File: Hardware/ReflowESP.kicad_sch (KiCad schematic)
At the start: 64 parts, among them J1 V_SSR_SEL, J2 USB_B_Micro, J3 SSR1, J4 EXT_V_SSR, J5 SSR2, J6 SSR3, J7 TC1, J8 TC2, Q1 BSS138, Q2 BSS138, Q3 S8050, Q4 S8050, Q5 BSS138, SW1 SW_RESET, SW2 SW_BOOT, U1 CH340G, U2 NCP1117-3.3_SOT223, U4 MAX31855KASA, U5 MAX31855KASA, Y1 12MHz

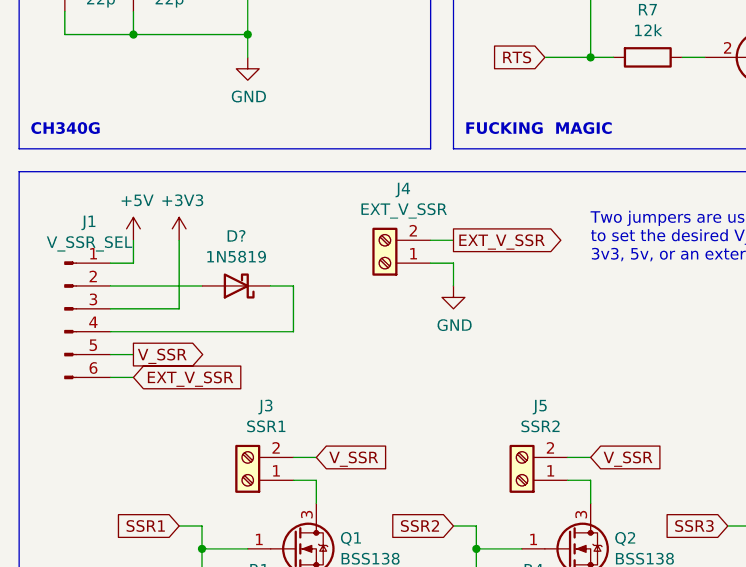
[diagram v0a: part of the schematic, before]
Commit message: Fix V_SSR_SEL
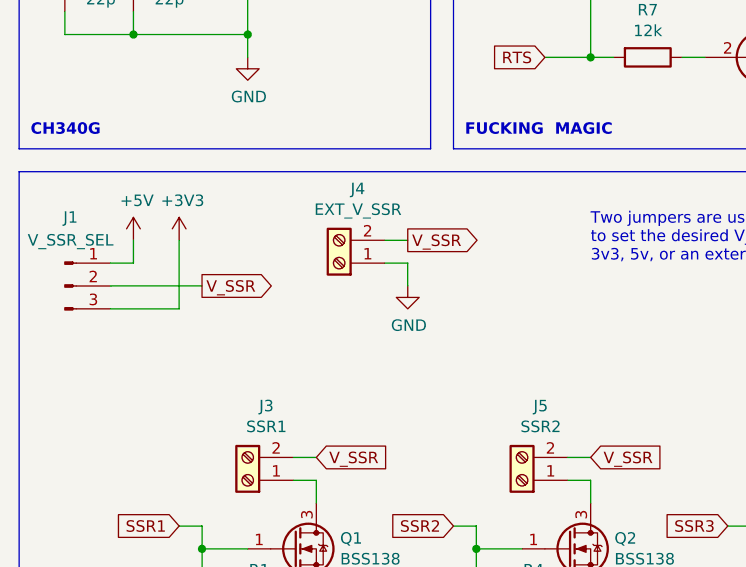
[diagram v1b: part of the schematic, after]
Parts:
- removed D?: 1N5819, Diode_THT:D_DO-41_SOD81_P10.16mm_Horizontal, symbol Diode:1N5819
- removed J1: V_SSR_SEL, symbol Connector:Conn_01x06_Male
- added J1: V_SSR_SEL, symbol Connector:Conn_01x03_Male
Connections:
- net EXT_V_SSR is gone; now on net V_SSR: J4.2 (Pin_2)
- net +3V3: now also J1.3 (Pin_3)
- net +5V: now also J1.1 (Pin_1)
- net V_SSR: now also J1.2 (Pin_2)
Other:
- moved on the sheet: J4
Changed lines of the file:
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@@
-    (stroke (width 0) (type default) (color 0 0 0 0))
-  )
-  (wire (pts (xy 40.64 149.86) (xy 43.18 149.86))
     (stroke (width 0) (type default) (color 0 0 0 0))
   )
@@
     (stroke (width 0) (type default) (color 0 0 0 0))
   )
-  (wire (pts (xy 60.96 147.32) (xy 60.96 149.86))
+  (wire (pts (xy 55.88 147.32) (xy 55.88 149.86))
     (stroke (width 0) (type default) (color 0 0 0 0))
   )
@@
     (stroke (width 0) (type default) (color 0 0 0 0))
   )
-  (wire (pts (xy 25.4 157.48) (xy 22.86 157.48))
-    (stroke (width 0) (type default) (color 0 0 0 0))
-  )
   (wire (pts (xy 200.66 91.44) (xy 203.2 91.44))
     (stroke (width 0) (type default) (color 0 0 0 0))
   )
-  (wire (pts (xy 58.42 147.32) (xy 60.96 147.32))
+  (wire (pts (xy 53.34 147.32) (xy 55.88 147.32))
     (stroke (width 0) (type default) (color 0 0 0 0))
   )
@@
     (stroke (width 0) (type default) (color 0 0 0 0))
   )
-  (wire (pts (xy 22.86 154.94) (xy 43.18 154.94))
-    (stroke (width 0) (type default) (color 0 0 0 0))
-  )
   (wire (pts (xy 45.72 186.69) (xy 45.72 189.23))
     (stroke (width 0) (type default) (color 0 0 0 0))
@@
     (stroke (width 0) (type default) (color 0 0 0 0))
   )
-  (wire (pts (xy 43.18 149.86) (xy 43.18 154.94))
-    (stroke (width 0) (type default) (color 0 0 0 0))
-  )
   (wire (pts (xy 33.02 25.4) (xy 43.18 25.4))
     (stroke (width 0) (type default) (color 0 0 0 0))
@@
     (stroke (width 0) (type default) (color 0 0 0 0))
   )
-  (wire (pts (xy 25.4 160.02) (xy 22.86 160.02))
-    (stroke (width 0) (type default) (color 0 0 0 0))
-  )
   (wire (pts (xy 17.78 111.76) (xy 17.78 114.3))
     (stroke (width 0) (type default) (color 0 0 0 0))
@@
     (stroke (width 0) (type default) (color 0 0 0 0))
   )
-  (wire (pts (xy 60.96 144.78) (xy 58.42 144.78))
+  (wire (pts (xy 55.88 144.78) (xy 53.34 144.78))
     (stroke (width 0) (type default) (color 0 0 0 0))
   )
@@
     )
   )
-  (global_label "EXT_V_SSR" (shape input) (at 25.4 160.02 0) (fields_autoplaced)
-    (effects (font (size 1.27 1.27)) (justify left))
-    (property "Intersheet References" "${INTERSHEET_REFS}" (id 0) (at -5.08 0 0)
-      (effects (font (size 1.27 1.27)) hide)
-    )
-  )
   (global_label "EN" (shape output) (at 109.22 53.34 0) (fields_autoplaced)
     (effects (font (size 1.27 1.27)) (justify left))
@@
     (effects (font (size 1.27 1.27)) (justify right))
     (property "Intersheet References" "${INTERSHEET_REFS}" (id 0) (at 5.08 0 0)
+      (effects (font (size 1.27 1.27)) hide)
+    )
+  )
+  (global_label "V_SSR" (shape output) (at 55.88 144.78 0) (fields_autoplaced)
+    (effects (font (size 1.27 1.27)) (justify left))
+    (property "Intersheet References" "${INTERSHEET_REFS}" (id 0) (at 25.4 -12.7 0)
       (effects (font (size 1.27 1.27)) hide)
     )
@@
     )
   )
-  (global_label "EXT_V_SSR" (shape output) (at 60.96 144.78 0) (fields_autoplaced)
-    (effects (font (size 1.27 1.27)) (justify left))
-    (property "Intersheet References" "${INTERSHEET_REFS}" (id 0) (at -5.08 0 0)
-      (effects (font (size 1.27 1.27)) hide)
-    )
-  )
   (global_label "CS0" (shape output) (at 132.08 144.78 180) (fields_autoplaced)
     (effects (font (size 1.27 1.27)) (justify right))
@@
     )
   )
-  (global_label "V_SSR" (shape output) (at 25.4 157.48 0) (fields_autoplaced)
-    (effects (font (size 1.27 1.27)) (justify left))
-    (property "Intersheet References" "${INTERSHEET_REFS}" (id 0) (at -5.08 0 0)
+  (global_label "V_SSR" (shape output) (at 33.02 149.86 0) (fields_autoplaced)
+    (effects (font (size 1.27 1.27)) (justify left))
+    (property "Intersheet References" "${INTERSHEET_REFS}" (id 0) (at 2.54 -7.62 0)
       (effects (font (size 1.27 1.27)) hide)
     )
@@
     (pin "7")
   )
-  (symbol (lib_id "Connector:Screw_Terminal_01x02") (at 53.34 147.32 180) (unit 1)
-    (in_bom yes) (on_board yes)
-    (property "Reference" "J4" (id 0) (at 55.4228 139.065 0))
-    (property "Value" "EXT_V_SSR" (id 1) (at 55.4228 141.3764 0))
-    (property "Footprint" "" (id 2) (at 53.34 147.32 0)
-      (effects (font (size 1.27 1.27)) hide)
-    )
-    (property "Datasheet" "~" (id 3) (at 53.34 147.32 0)
-      (effects (font (size 1.27 1.27)) hide)
-    )
-    (pin "1")
-    (pin "2")
-  )
-  (symbol (lib_id "power:GND") (at 60.96 149.86 0) (unit 1)
-    (in_bom yes) (on_board yes)
-    (property "Reference" "#PWR010" (id 0) (at 60.96 156.21 0)
-      (effects (font (size 1.27 1.27)) hide)
-    )
-    (property "Value" "GND" (id 1) (at 61.087 154.2542 0))
-    (property "Footprint" "" (id 2) (at 60.96 149.86 0)
-      (effects (font (size 1.27 1.27)) hide)
-    )
-    (property "Datasheet" "" (id 3) (at 60.96 149.86 0)
+  (symbol (lib_id "Connector:Screw_Terminal_01x02") (at 48.26 147.32 180) (unit 1)
+    (in_bom yes) (on_board yes)
+    (property "Reference" "J4" (id 0) (at 50.3428 139.065 0))
+    (property "Value" "EXT_V_SSR" (id 1) (at 50.3428 141.3764 0))
+    (property "Footprint" "" (id 2) (at 48.26 147.32 0)
+      (effects (font (size 1.27 1.27)) hide)
+    )
+    (property "Datasheet" "~" (id 3) (at 48.26 147.32 0)
+      (effects (font (size 1.27 1.27)) hide)
+    )
+    (pin "1")
+    (pin "2")
+  )
+  (symbol (lib_id "power:GND") (at 55.88 149.86 0) (unit 1)
+    (in_bom yes) (on_board yes)
+    (property "Reference" "#PWR010" (id 0) (at 55.88 156.21 0)
+      (effects (font (size 1.27 1.27)) hide)
+    )
+    (property "Value" "GND" (id 1) (at 56.007 154.2542 0))
+    (property "Footprint" "" (id 2) (at 55.88 149.86 0)
+      (effects (font (size 1.27 1.27)) hide)
+    )
+    (property "Datasheet" "" (id 3) (at 55.88 149.86 0)
       (effects (font (size 1.27 1.27)) hide)
     )
@@
     (pin "2")
   )
-  (symbol (lib_id "Diode:1N5819") (at 36.83 149.86 180) (unit 1)
-    (in_bom yes) (on_board yes)
-    (property "Reference" "D?" (id 0) (at 36.83 144.3482 0))
-    (property "Value" "1N5819" (id 1) (at 36.83 146.6596 0))
-    (property "Footprint" "Diode_THT:D_DO-41_SOD81_P10.16mm_Horizontal" (id 2) (at 36.83 145.415 0)
-      (effects (font (size 1.27 1.27)) hide)
-    )
-    (property "Datasheet" "http://www.vishay.com/docs/88525/1n5817.pdf" (id 3) (at 36.83 149.86 0)
-      (effects (font (size 1.27 1.27)) hide)
-    )
-    (pin "1")
-    (pin "2")
-  )
   (symbol (lib_id "Device:C_Small") (at 246.38 58.42 90) (unit 1)
     (in_bom yes) (on_board yes)
@@
     (pin "2")
   )
-  (symbol (lib_id "Connector:Conn_01x06_Male") (at 17.78 152.4 0) (unit 1)
-    (in_bom yes) (on_board yes)
-    (property "Reference" "J1" (id 0) (at 20.5232 142.7226 0))
-    (property "Value" "V_SSR_SEL" (id 1) (at 20.5232 145.034 0))
-    (property "Footprint" "" (id 2) (at 17.78 152.4 0)
-      (effects (font (size 1.27 1.27)) hide)
-    )
-    (property "Datasheet" "~" (id 3) (at 17.78 152.4 0)
-      (effects (font (size 1.27 1.27)) hide)
-    )
-    (pin "1")
-    (pin "2")
-    (pin "3")
-    (pin "4")
-    (pin "5")
-    (pin "6")
-  )
   (symbol (lib_id "Device:R") (at 264.16 107.95 0) (unit 1)
     (in_bom yes) (on_board yes)
@@
     (pin "1")
     (pin "2")
+  )
+  (symbol (lib_id "Connector:Conn_01x03_Male") (at 17.78 149.86 0) (unit 1)
+    (in_bom yes) (on_board yes) (fields_autoplaced)
+    (property "Reference" "J1" (id 0) (at 18.415 142.24 0))
+    (property "Value" "V_SSR_SEL" (id 1) (at 18.415 144.78 0))
+    (property "Footprint" "" (id 2) (at 17.78 149.86 0)
+      (effects (font (size 1.27 1.27)) hide)
+    )
+    (property "Datasheet" "~" (id 3) (at 17.78 149.86 0)
+      (effects (font (size 1.27 1.27)) hide)
+    )
+    (pin "1")
+    (pin "2")
+    (pin "3")
   )
   (symbol (lib_id "Connector_Generic:Conn_01x02") (at 48.26 25.4 0) (unit 1)
@@
       (reference "D3") (unit 1) (value "LED") (footprint "")
     )
-    (path "/00000000-0000-0000-0000-00006188625a"
-      (reference "D?") (unit 1) (value "1N5819") (footprint "Diode_THT:D_DO-41_SOD81_P10.16mm_Horizontal")
-    )
     (path "/2fe28d3e-2539-4dbf-944b-18ec831c57d3"
       (reference "H?") (unit 1) (value "MountingHole_Pad") (footprint "")
@@
       (reference "H?") (unit 1) (value "MountingHole_Pad") (footprint "")
     )
-    (path "/00000000-0000-0000-0000-000061aed84c"
+    (path "/0ab28289-de97-4674-94d7-6755b58bc81c"
       (reference "J1") (unit 1) (value "V_SSR_SEL") (footprint "")
     )

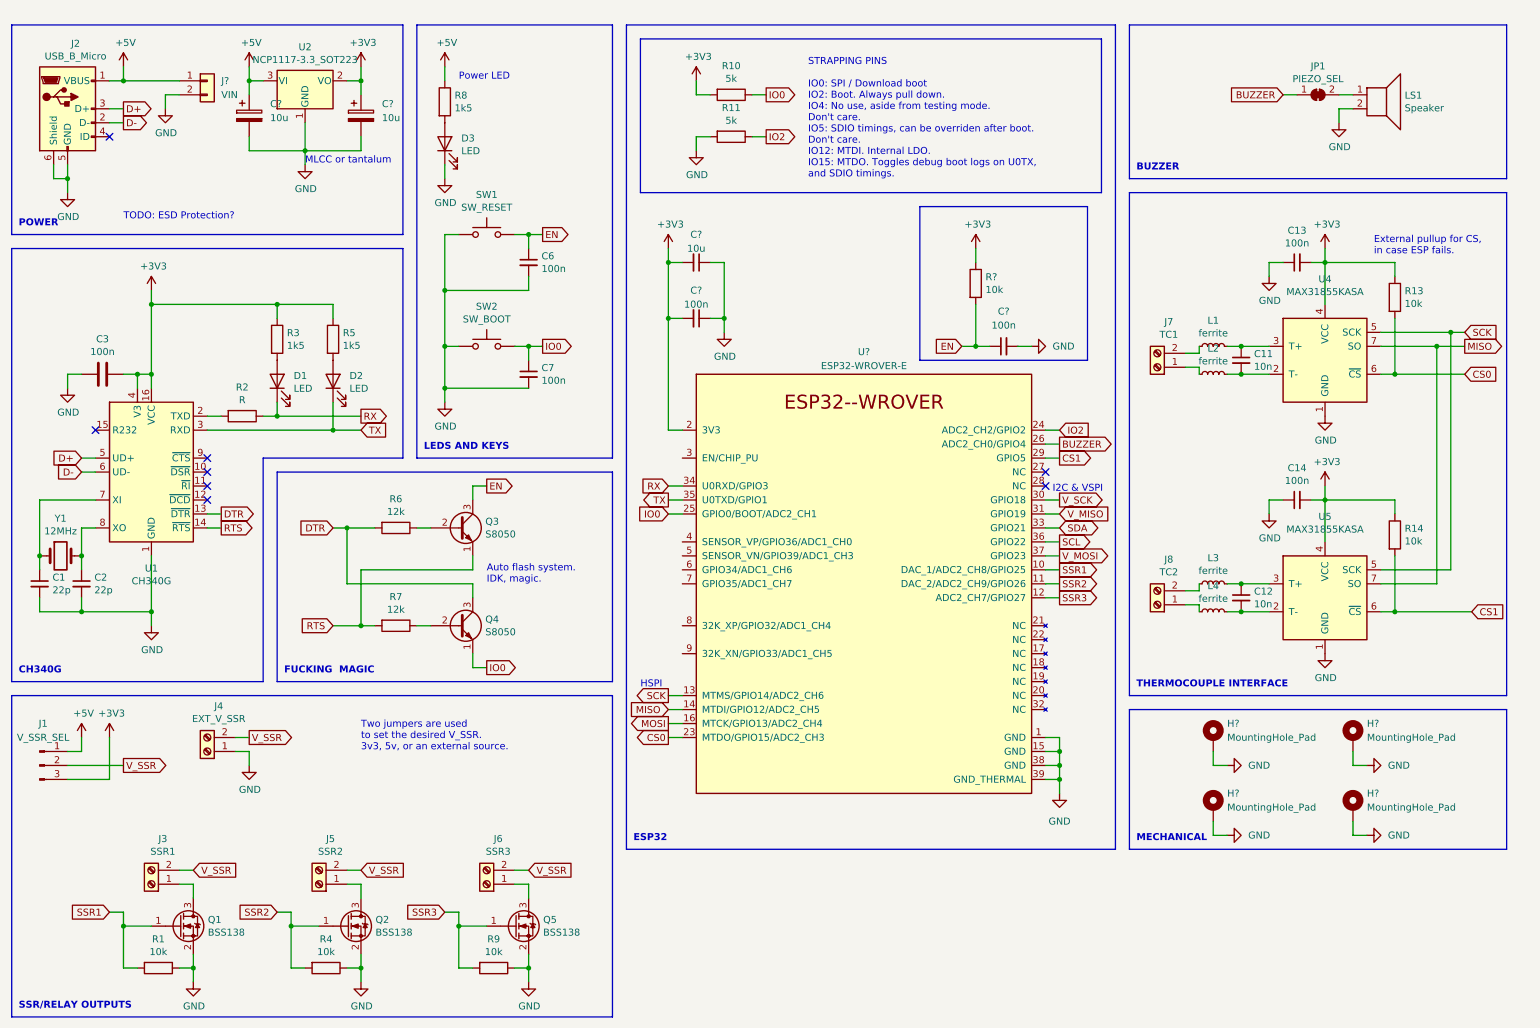
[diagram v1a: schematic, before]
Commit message: Small tweaks for v0.0.4
Remove USB-UART
Add connections for programming, display and servo
Add gate resistor for SSRs
More filter caps for 3v3
Update refs and footprints
Fix symbol for ESP32 module
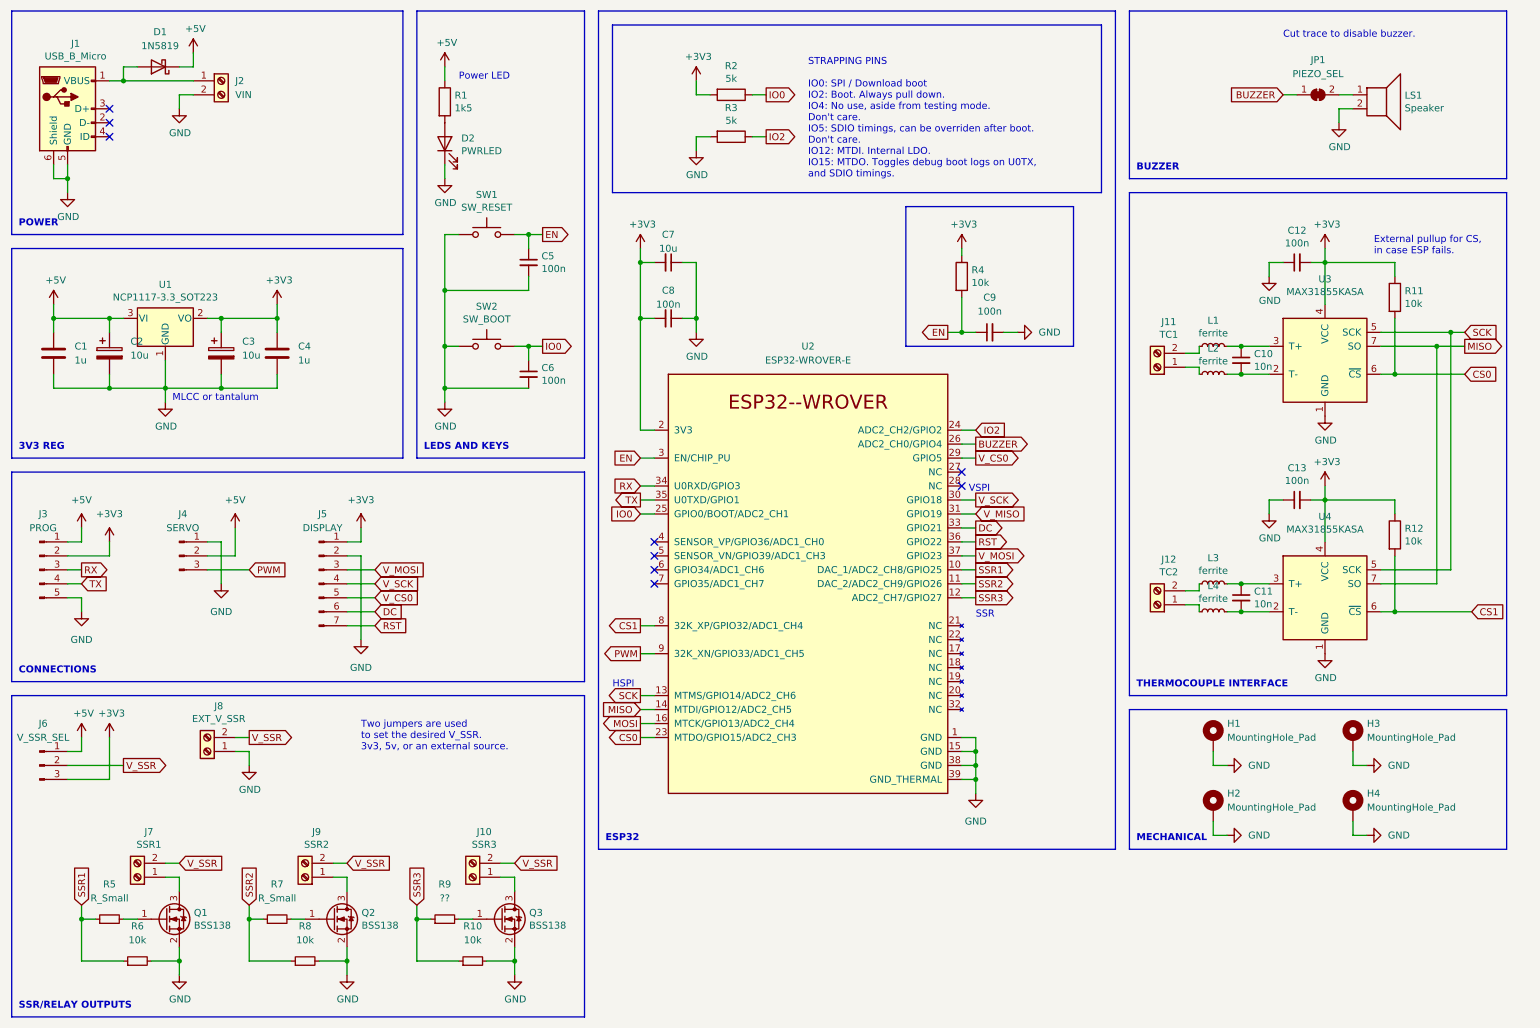
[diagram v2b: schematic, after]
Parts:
- removed C1, C2: 22p, symbol Device:C_Small
- removed C3: 100n, symbol Device:C
- removed D1, D2: LED, symbol Device:LED
- removed J?: VIN, symbol Connector_Generic:Conn_01x02
- removed Q3, Q4: S8050, Package_TO_SOT_THT:TO-92_Inline, symbol Transistor_BJT:S8050
- removed R1, R4, R9: 10k, symbol Device:R
- removed R2: R, symbol Device:R
- removed R3, R5: 1k5, symbol Device:R
- removed R6, R7: 12k, symbol Device:R
- removed U1: CH340G, Package_SO:SOIC-16_3.9x9.9mm_P1.27mm, symbol Interface_USB:CH340G
- removed U?: ESP32-WROVER-E, Espressif:ESP32-WROVER-E, symbol Espressif:ESP32-WROVER-E
- removed Y1: 12MHz, symbol Device:Crystal
- added C1, C4: 1u, Capacitor_SMD:C_0805_2012Metric, symbol Device:C
- added D1: 1N5819, Diode_SMD:D_SOD-323, symbol Device:D_Schottky
- added J2: VIN, symbol Connector:Screw_Terminal_01x02
- added J3: PROG, Connector_PinHeader_2.54mm:PinHeader_1x05_P2.54mm_Vertical, symbol Connector:Conn_01x05_Male
- added J4: SERVO, Connector_PinHeader_2.54mm:PinHeader_1x03_P2.54mm_Horizontal, symbol Connector:Conn_01x03_Male
- added J5: DISPLAY, Connector_PinHeader_2.54mm:PinHeader_1x07_P2.54mm_Horizontal, symbol Connector:Conn_01x07_Male
- added R10, R6, R8: 10k, Resistor_SMD:R_0805_2012Metric, symbol Device:R_Small
- added R5, R7: R_Small, Resistor_SMD:R_0805_2012Metric, symbol Device:R_Small
- added R9: ??, Resistor_SMD:R_0805_2012Metric, symbol Device:R_Small
- added U2: ESP32-WROVER-E, Espressif:ESP32-WROVER-E, symbol Espressif:ESP32-WROVER-E
- C10: renamed from C11; footprint (none) -> Capacitor_SMD:C_0805_2012Metric
- C11: renamed from C12; footprint (none) -> Capacitor_SMD:C_0805_2012Metric
- C12: renamed from C13; footprint (none) -> Capacitor_SMD:C_0805_2012Metric
- C13: renamed from C14; footprint (none) -> Capacitor_SMD:C_0805_2012Metric
- C5: renamed from C6; footprint (none) -> Capacitor_SMD:C_0805_2012Metric
- C6: renamed from C7; footprint (none) -> Capacitor_SMD:C_0805_2012Metric
- C7, C8, C9: renamed from C?; footprint (none) -> Capacitor_SMD:C_0805_2012Metric
- D2: renamed from D3; value LED -> PWRLED; footprint (none) -> LED_SMD:LED_0805_2012Metric
- H1, H2, H3, H4: renamed from H?; footprint (none) -> MountingHole:MountingHole_3.2mm_M3_Pad
- J6: renamed from J1; footprint (none) -> Connector_PinHeader_2.54mm:PinHeader_1x03_P2.54mm_Vertical
- JP1: footprint (none) -> Jumper:SolderJumper-2_P1.3mm_Bridged2Bar_RoundedPad1.0x1.5mm
- R1: renamed from R8; footprint (none) -> Resistor_SMD:R_0805_2012Metric
- R11: renamed from R13; footprint (none) -> Resistor_SMD:R_0805_2012Metric
- R12: renamed from R14; footprint (none) -> Resistor_SMD:R_0805_2012Metric
- R2: renamed from R10; footprint (none) -> Resistor_SMD:R_0805_2012Metric
- R3: renamed from R11; footprint (none) -> Resistor_SMD:R_0805_2012Metric
- R4: renamed from R?; footprint (none) -> Resistor_SMD:R_0805_2012Metric
- gave numbers to parts that had none: 2
- renumbered J2 to J1, J6 to J10, J7 to J11, J8 to J12, J3 to J7, J4 to J8, J5 to J9, Q5 to Q3, U2 to U1, U4 to U3, U5 to U4
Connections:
- net +3V3: now also C4.1, J3.2 (Pin_2), J5.1 (Pin_1), U2.2 (3V3)
- net +5V: now also C1.1, D1.1 (K), J3.1 (Pin_1), J4.2 (Pin_2); no longer J1.1 (VBUS)
- net BUZZER: now also U2.26 (ADC2_CH0/GPIO4)
- net CS0: now also U2.23 (MTDO/GPIO15/ADC2_CH3)
- net CS1: now also U2.8 (32K_XP/GPIO32/ADC1_CH4)
- net EN: now also U2.3 (EN/CHIP_PU)
- net GND: now also C1.2, C4.2, J2.2 (Pin_2), J3.5 (Pin_5), J4.1 (Pin_1), J5.2 (Pin_2), R10.2, R6.2, R8.2, U2.1 (GND), U2.15 (GND), U2.38 (GND), U2.39 (GND_THERMAL)
- net IO0: now also U2.25 (GPIO0/BOOT/ADC2_CH1)
- net IO2: now also U2.24 (ADC2_CH2/GPIO2)
- net MISO: now also U2.14 (MTDI/GPIO12/ADC2_CH5)
- net MOSI: now also U2.16 (MTCK/GPIO13/ADC2_CH4)
- net RX: now also J3.3 (Pin_3), U2.34 (U0RXD/GPIO3)
- net SCK: now also U2.13 (MTMS/GPIO14/ADC2_CH6)
- net SSR1: now also R5.1, R6.1, U2.10 (DAC_1/ADC2_CH8/GPIO25); no longer Q1.1 (G)
- net SSR2: now also R7.1, R8.1, U2.11 (DAC_2/ADC2_CH9/GPIO26); no longer Q2.1 (G)
- net SSR3: now also R10.1, R9.1, U2.12 (ADC2_CH7/GPIO27); no longer Q3.1 (G)
- net TX: now also J3.4 (Pin_4), U2.35 (U0TXD/GPIO1)
- net V_MISO: now also U2.31 (GPIO19)
- net V_MOSI: now also J5.3 (Pin_3), U2.37 (GPIO23)
- net V_SCK: now also J5.4 (Pin_4), U2.30 (GPIO18)
- net D+: no longer names the net of J1.3 (D+)
- net D-: no longer names the net of J1.2 (D-)
- new net: D1.2 (A), J1.1 (VBUS), J2.1 (Pin_1)
- new net: Q2.1 (G), R7.2
- new net: Q1.1 (G), R5.2
- new net: Q3.1 (G), R9.2
- new net DC: J5.6 (Pin_6), U2.33 (GPIO21)
- new net PWM: J4.3 (Pin_3), U2.9 (32K_XN/GPIO33/ADC1_CH5)
- new net RST: J5.7 (Pin_7), U2.36 (GPIO22)
- new net V_CS0: J5.5 (Pin_5), U2.29 (GPIO5)
- no-connect marks 8 -> 9
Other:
- note added: "3V3 REG"
- note added: "CONNECTIONS"
- note added: "Cut trace to disable buzzer."
- note added: "SSR"
- note added: "VSPI"
- note removed: "Auto flash system. IDK, magic."
- note removed: "CH340G"
- note removed: "FUCKING MAGIC"
- note removed: "I2C & VSPI"
- note removed: "TODO: ESD Protection?"
- moved on the sheet: C2, C3, C7, C8, C9, J10, J7, J9, Q1, Q2, Q3, R4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
